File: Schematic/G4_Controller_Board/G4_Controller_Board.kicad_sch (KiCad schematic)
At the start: 49 parts, among them J1 Rev Trigger (Optional), J10 Solenoid, J11 Inter-board Jumper, J12 Inter-board Jumper, J13 IR LED Rec., J14 IR Led Emitter, J15 IR LED Rec., J16 IR LED Emitter, J17 Positive BUS, J18 Negative BUS, J2 ESC Right, J3 ESC Left, J4 Fire Trigger, J5 Magazine Removal Trigger, J6 Rev Trigger (Optional), J7 Fire Trigger, J8 Magazine Removal Trigger, J9 I2C Out, Q1 2N7000, Q5 Q_NMOS_GDS, Q6 Q_PMOS_GDS, SW1 Rev Switch, SW2 Preset A, SW3 Preset B, SW4 Preset C, SW5 Fire Switch, SW6 MagRemovalSwitch, SW7 RotaryEncoder_Switch, U1 ESP32-LOLIN32-Lite, U2 Mini360

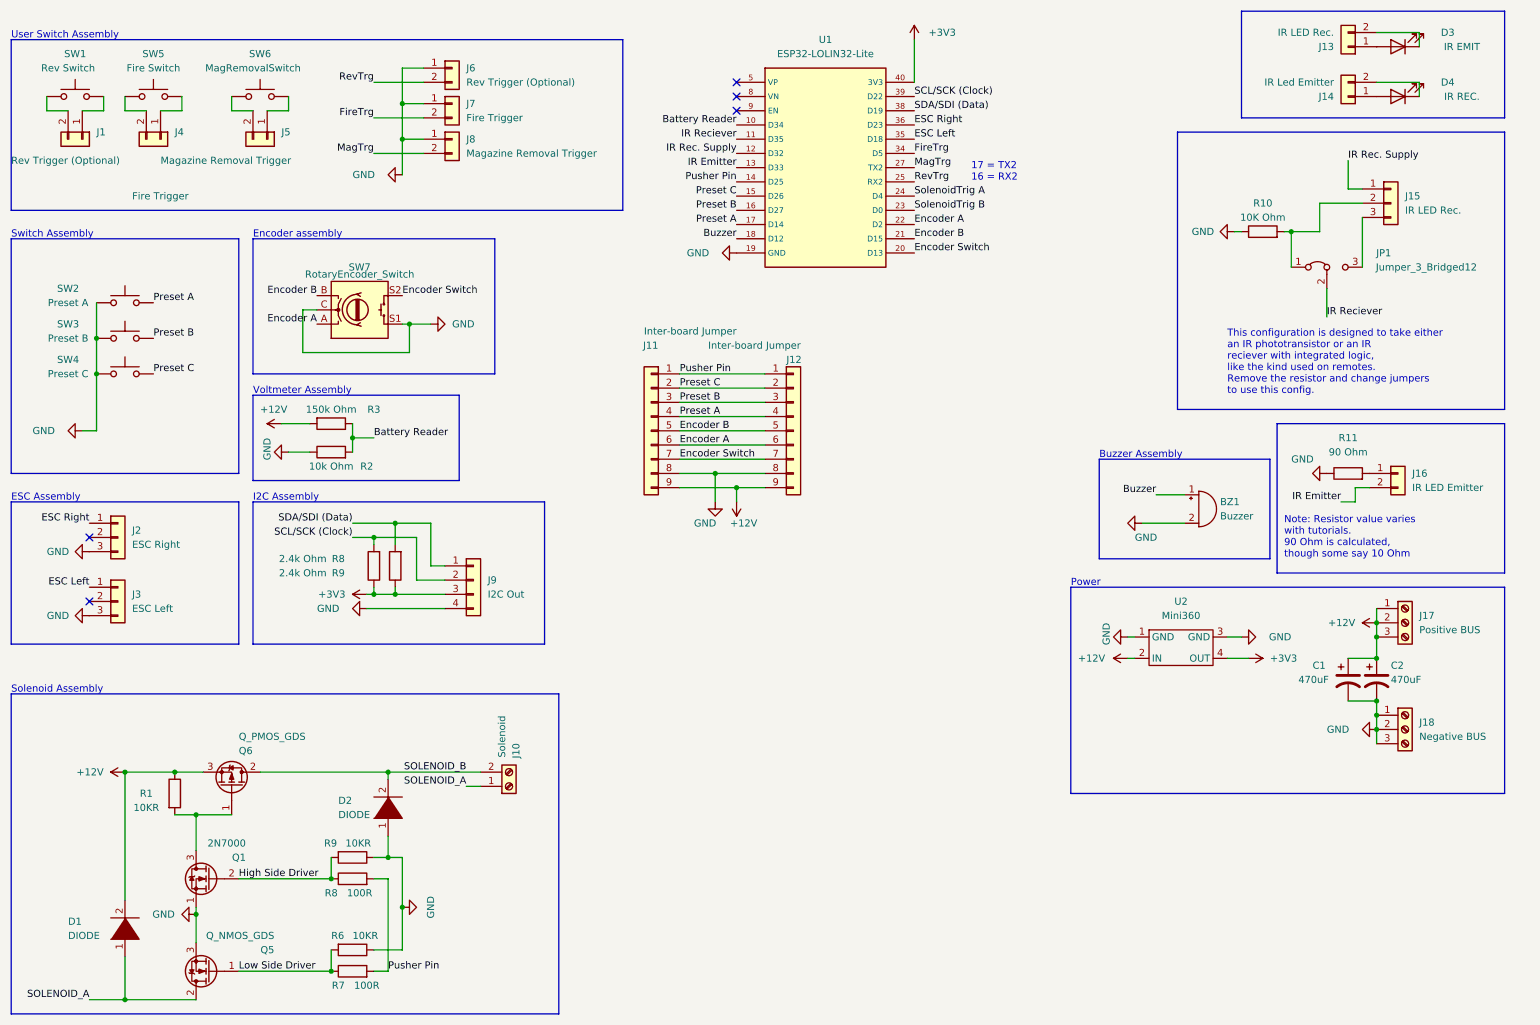
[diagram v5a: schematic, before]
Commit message: update PCB model
progress on logic-side board
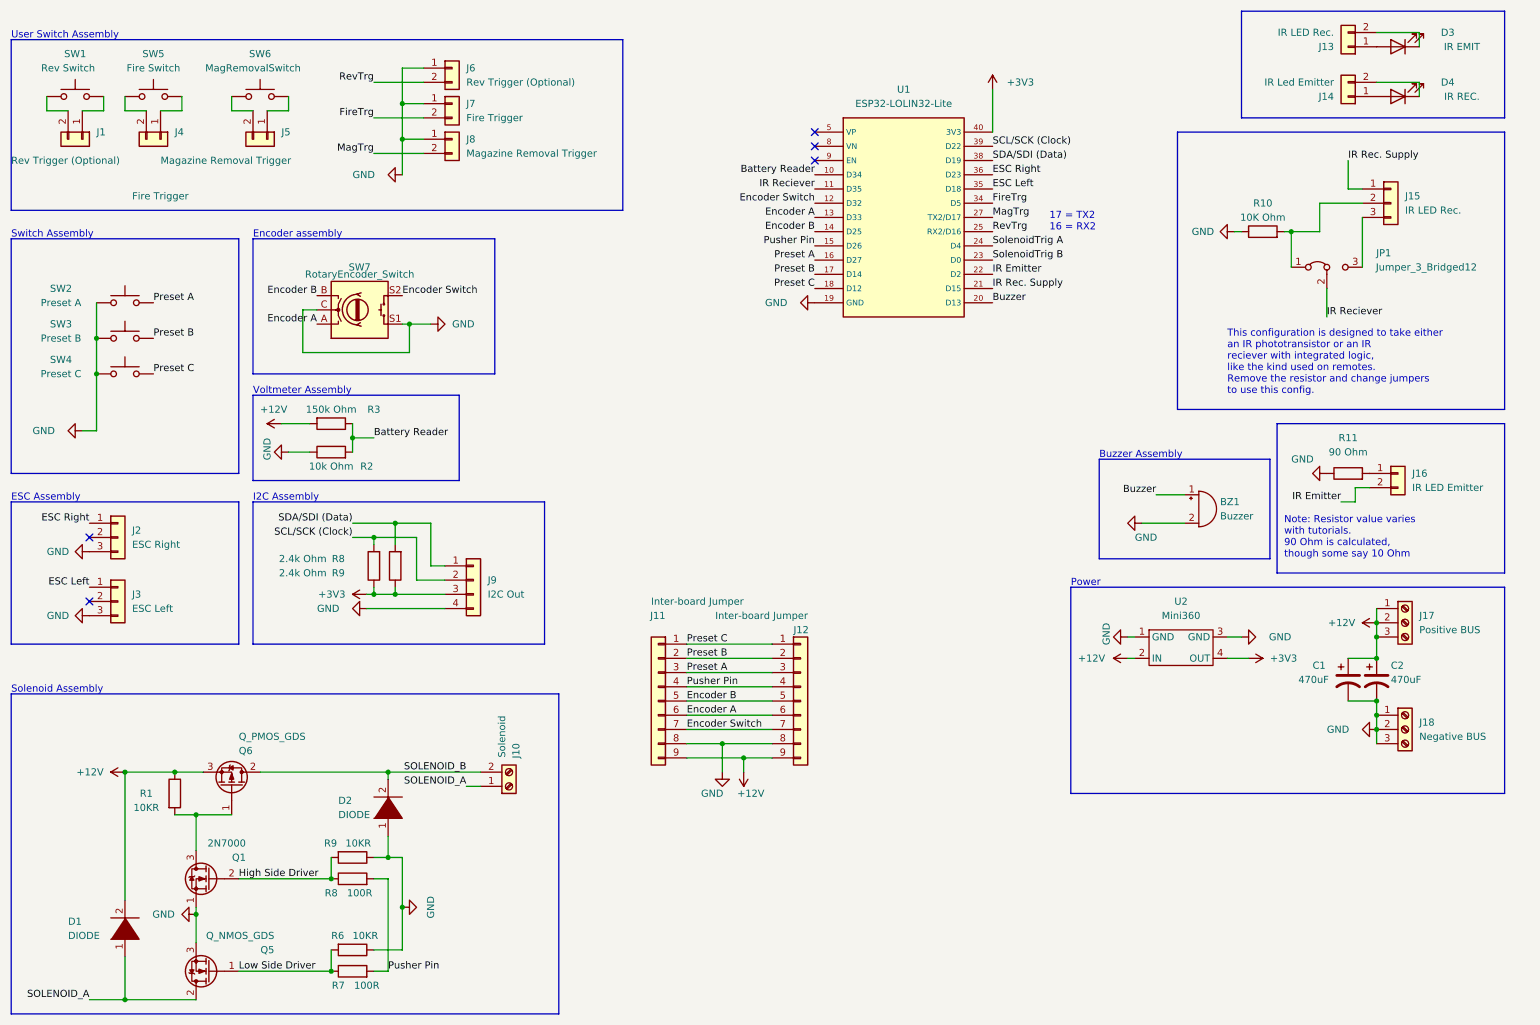
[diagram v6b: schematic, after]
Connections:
- net Buzzer: now also U1.20 (D13); no longer U1.18 (D12)
- net Encoder A: now also U1.13 (D33); no longer U1.22 (D2)
- net Encoder B: now also U1.14 (D25); no longer U1.21 (D15)
- net Encoder Switch: now also U1.12 (D32); no longer U1.20 (D13)
- net GND: now also SW2.2, SW3.2, SW4.2; no longer SW2.1, SW3.1, SW4.1
- net IR Emitter: now also U1.22 (D2); no longer U1.13 (D33)
- net IR Rec. Supply: now also U1.21 (D15); no longer U1.12 (D32)
- net Preset A: now also J11.3 (Pin_3), J12.3 (Pin_3), SW2.1, U1.16 (D27); no longer J11.4 (Pin_4), J12.4 (Pin_4), SW2.2, U1.17 (D14)
- net Preset B: now also J11.2 (Pin_2), J12.2 (Pin_2), SW3.1, U1.17 (D14); no longer J11.3 (Pin_3), J12.3 (Pin_3), SW3.2, U1.16 (D27)
- net Preset C: now also J11.1 (Pin_1), J12.1 (Pin_1), SW4.1, U1.18 (D12); no longer J11.2 (Pin_2), J12.2 (Pin_2), SW4.2, U1.15 (D26)
- net Pusher Pin: now also J11.4 (Pin_4), J12.4 (Pin_4), U1.15 (D26); no longer J11.1 (Pin_1), J12.1 (Pin_1), U1.14 (D25)
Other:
- moved on the sheet: J11, J12, U1

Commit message: update kicad schematic
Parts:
- removed J6: Rev Trigger (Optional), Connector_PinSocket_2.54mm:PinSocket_1x02_P2.54mm_Vertical, symbol Connector_Generic:Conn_01x02
- removed J7: Fire Trigger, Connector_PinSocket_2.54mm:PinSocket_1x02_P2.54mm_Vertical, symbol Connector_Generic:Conn_01x02
- removed J8: Magazine Removal Trigger, Connector_PinSocket_2.54mm:PinSocket_1x02_P2.54mm_Vertical, symbol Connector_Generic:Conn_01x02
- added J6: Rev Trigger (Optional), Connector_PinHeader_2.54mm:PinHeader_1x03_P2.54mm_Vertical, symbol Connector_Generic:Conn_01x03
- added J7: Fire Trigger, Connector_PinHeader_2.54mm:PinHeader_1x03_P2.54mm_Vertical, symbol Connector_Generic:Conn_01x03
- added J8: Magazine Removal Trigger, Connector_PinHeader_2.54mm:PinHeader_1x03_P2.54mm_Vertical, symbol Connector_Generic:Conn_01x03
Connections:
- net FireTrg: now also J7.3 (Pin_3)
- net GND: now also J6.1 (Pin_1), J6.2 (Pin_2), J7.1 (Pin_1), J7.2 (Pin_2), J8.1 (Pin_1), J8.2 (Pin_2)
- net MagTrg: now also J8.3 (Pin_3)
- net RevTrg: now also J6.3 (Pin_3)
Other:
- note removed: "17 = TX2 16 = RX2"

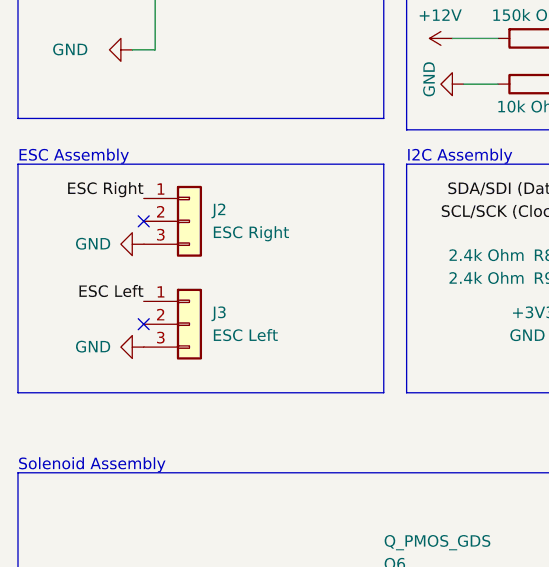
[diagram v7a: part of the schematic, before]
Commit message: try 3 flywheel mount
tried single piece flywheel mount, but that resulted in print issues, so I'm trying a different method that uses more bolts. Also updated other things such as the PCB.
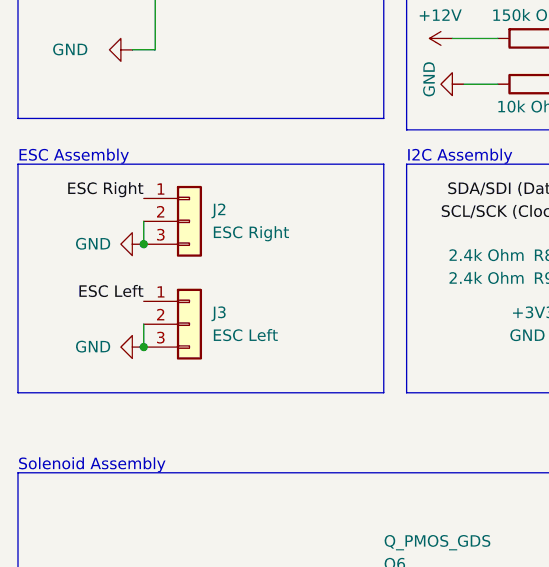
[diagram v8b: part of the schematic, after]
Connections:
- net GND: now also J2.2 (Pin_2), J3.2 (Pin_2)
- no-connect marks 5 -> 3
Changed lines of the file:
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@@
   (junction (at 146.05 148.59) (diameter 0) (color 0 0 0 0)
   )
+  (junction (at 29.21 123.19) (diameter 0) (color 0 0 0 0)
+  )
   (junction (at 83.82 106.68) (diameter 0) (color 0 0 0 0)
   )
@@
   )
   (junction (at 142.24 146.05) (diameter 0) (color 0 0 0 0)
+  )
+  (junction (at 29.21 111.76) (diameter 0) (color 0 0 0 0)
   )
   (no_connect (at 158.75 39.37))
   (no_connect (at 158.75 41.91))
   (no_connect (at 158.75 36.83))
-  (no_connect (at 29.21 109.22))
-  (no_connect (at 29.21 120.65))
   (wire (pts (xy 60.96 33.02) (xy 64.77 33.02))
     (stroke (width 0) (type default))
@@
     (stroke (width 0) (type default))
   )
+  (wire (pts (xy 29.21 109.22) (xy 29.21 111.76))
+    (stroke (width 0) (type default))
+  )
   (wire (pts (xy 55.88 186.69) (xy 72.39 186.69))
     (stroke (width 0) (type default))
@@
     (stroke (width 0) (type default))
   )
+  (wire (pts (xy 29.21 120.65) (xy 29.21 123.19))
+    (stroke (width 0) (type default))
+  )
